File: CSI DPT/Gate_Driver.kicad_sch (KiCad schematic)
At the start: 21 parts, among them J1 CT3151SP-0, J2 CT3151SP-0, U1 UCC23513QDWYRQ1, U2 MGJ2D051802SC, U3 MGJ2D051802SC, U4 LDK130-12_SOT23_SOT353, U5 NC7SZ125M5X

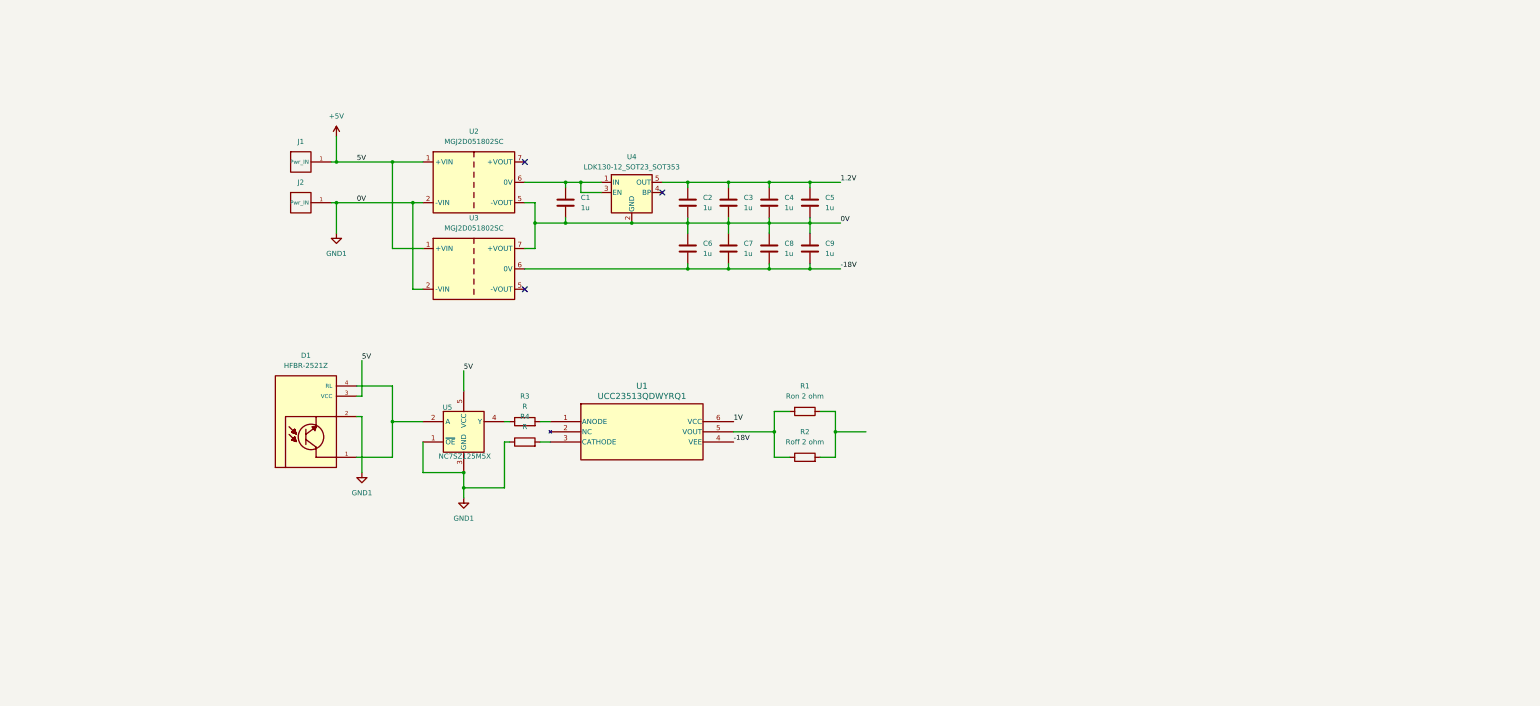
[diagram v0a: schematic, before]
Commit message: Nov.17 Update
Changed from opto PWM transmission to differential transmission. With added test point.
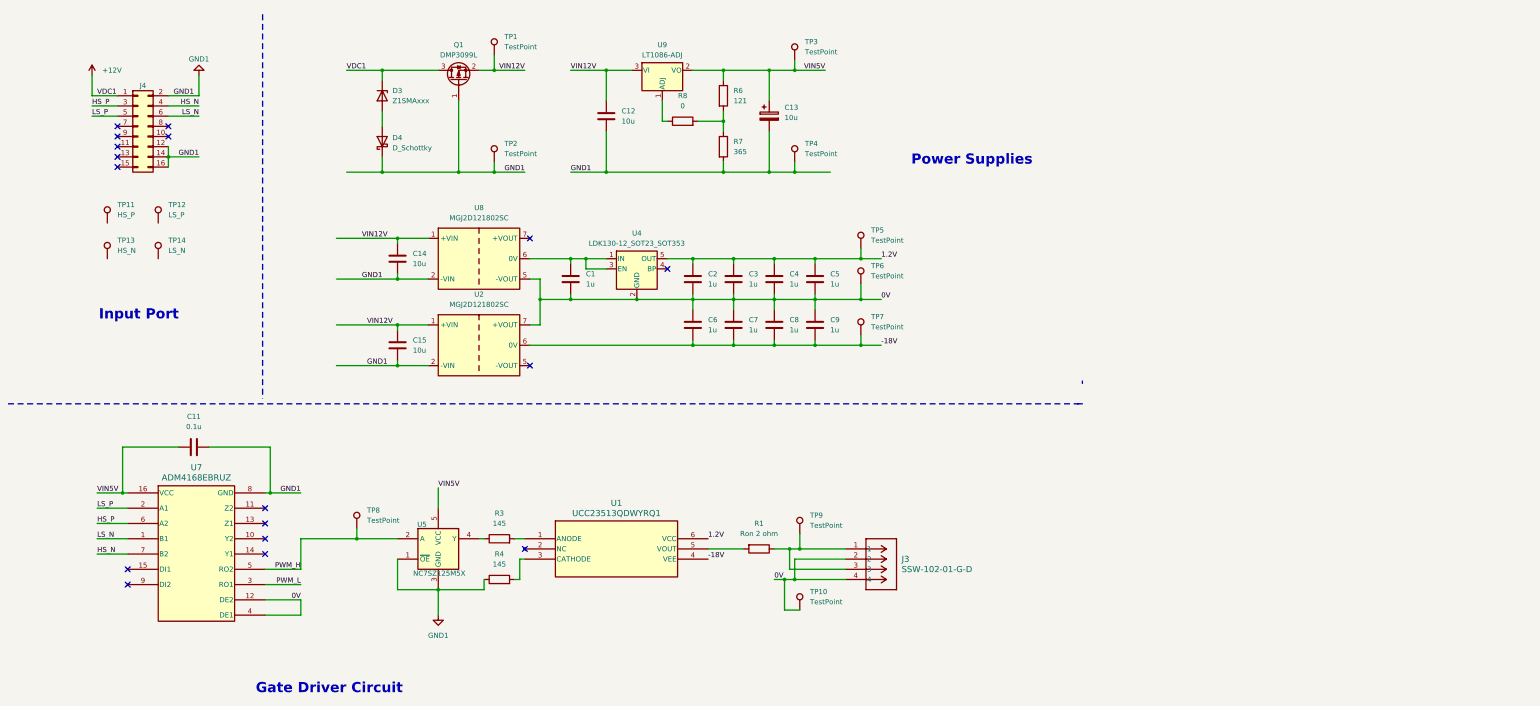
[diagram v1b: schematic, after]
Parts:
- removed D1: HFBR-2521Z, HFBR-2521Z:OPTO_HFBR-2521Z, symbol Opto_reciever:HFBR-2521Z
- removed J1, J2: CT3151SP-0, Connector:Banana_Jack_CT3151SP-0, symbol Connector:Banana_Jack_CT3151SP-0
- removed R2: Roff 2 ohm, symbol Device:R
- removed U2, U3: MGJ2D051802SC, Converter_DCDC:Converter_DCDC_Murata_MGJ2DxxxxxxSC_THT, symbol Converter_DCDC:MGJ2D051802SC
- added C11: 0.1u, symbol Device:C
- added C12: 10u, Capacitor_SMD:C_1206_3216Metric_Pad1.33x1.80mm_HandSolder, symbol Device:C
- added C13: 10u, symbol Device:C_Polarized
- added C14, C15: 10u, Capacitor_SMD:C_1206_3216Metric, symbol Device:C
- added D3: Z1SMAxxx, Diode_SMD:D_SMA_Handsoldering, symbol Diode:Z1SMAxxx
- added D4: D_Schottky, Diode_SMD:D_PowerDI-123, symbol Device:D_Schottky
- added J3: SSW-102-01-G-D, Gate_Driver:CON4_2X2_TU_SSQ, symbol 2*2_Gate_Driver_Output_Connector:SSW-102-01-G-D
- added J4: Conn_02x08_Odd_Even, Connector_IDC:IDC-Header_2x08_P2.54mm_Vertical, symbol Connector_Generic:Conn_02x08_Odd_Even
- added Q1: DMP3099L, Package_TO_SOT_SMD:SOT-23, symbol Transistor_FET:DMP3099L
- added R6: 121, Resistor_SMD:R_1206_3216Metric_Pad1.30x1.75mm_HandSolder, symbol Device:R
- added R7: 365, Resistor_SMD:R_1206_3216Metric_Pad1.30x1.75mm_HandSolder, symbol Device:R
- added R8: 0, Resistor_SMD:R_1206_3216Metric_Pad1.30x1.75mm_HandSolder, symbol Device:R
- added TP1: TestPoint, TestPoint:TestPoint_Pad_D2.0mm, symbol Connector:TestPoint
- added TP10, TP2, TP3, TP4, TP5, TP6, TP7, TP8, TP9: TestPoint, symbol Connector:TestPoint
- added TP11: HS_P, TestPoint:TestPoint_Pad_D2.0mm, symbol Connector:TestPoint
- added TP12: LS_P, TestPoint:TestPoint_Pad_D2.0mm, symbol Connector:TestPoint
- added TP13: HS_N, symbol Connector:TestPoint
- added TP14: LS_N, symbol Connector:TestPoint
- added U2, U8: MGJ2D121802SC, Converter_DCDC:Converter_DCDC_Murata_MGJ2DxxxxxxSC_THT, symbol Converter_DCDC:MGJ2D121802SC
- added U7: ADM4168EBRUZ, Gate_Driver:RU_16_ADI-M, symbol RS422_Transreciver:ADM4168EBRUZ
- added U9: LT1086-ADJ, symbol Regulator_Linear:LT1086-ADJ
- R1: footprint (none) -> Resistor_SMD:R_1206_3216Metric_Pad1.30x1.75mm_HandSolder
- R3, R4: value R -> 145; footprint Resistor_SMD:R_1206_3216Metric -> Resistor_SMD:R_1206_3216Metric_Pad1.30x1.75mm_HandSolder
- U1: footprint SOIC06_SO-6_7P5X4P68_TEX -> Gate_Driver:SOIC06_SO-6_7P5X4P68_TEX-M
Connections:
- net 1V is gone; now on net 1.2V: U1.6 (VCC)
- net -18V: now also TP7.1, U2.6 (0V)
- net 1.2V: now also TP5.1
- net GND1: now also C11.2, C12.2, C13.2, C14.2, C15.2, D4.1 (K), J4.12 (Pin_12), J4.14 (Pin_14), J4.16 (Pin_16), J4.2 (Pin_2), Q1.1 (G), R7.2, TP2.1, TP4.1, U2.2 (-VIN), U7.8 (GND), U8.2 (-VIN); no longer C1.2, C2.2, C3.2, C4.2, C5.2, C6.1, C7.1, C8.1, C9.1, U4.2 (GND)
- net at C1.1, U4.1 (IN), U4.3 (EN): now also U8.6 (0V)
- net at R1.1: now also J3.1, J3.3, TP9.1
- net PWM_H: now reaches U5.2 (A)
- net PWM_H: now also TP8.1, U7.5 (RO2)
- net +5V renamed VIN5V
- net VIN5V: now also C11.1, C13.1, R6.1, TP3.1, U7.16 (VCC), U9.2 (VO)
- new net: D3.2 (A), D4.2 (A)
- new net: R8.1, U9.1 (ADJ)
- new net: R6.2, R7.1, R8.2
- new net +12V: D3.1 (K), J4.1 (Pin_1), Q1.3 (D)
- new net 0V: C1.2, C2.2, C3.2, C4.2, C5.2, C6.1, C7.1, C8.1, C9.1, J3.2, J3.4, TP10.1, TP6.1, U2.7 (+VOUT), U4.2 (GND), U7.12 (DE2), U7.4 (DE1), U8.5 (-VOUT)
- new net HS_N: J4.4 (Pin_4), U7.7 (B2)
- new net HS_P: J4.3 (Pin_3), U7.6 (A2)
- new net LS_N: J4.6 (Pin_6), U7.1 (B1)
- new net LS_P: J4.5 (Pin_5), U7.2 (A1)
- new net PWM_L: U7.3 (RO1)
- new net VIN12V: C12.1, C14.1, C15.1, Q1.2 (S), TP1.1, U2.1 (+VIN), U8.1 (+VIN), U9.3 (VI)
- no-connect marks 3 -> 17
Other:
- note added: "Gate Driver Circuit"
- note added: "Input Port"
- note added: "Power Supplies"
- moved on the sheet: C1, C2, C3, C4, C5, C6, C7, C8, C9, R1, R3, R4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

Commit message: Nov.18 Update 1
temporary save
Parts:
- C11: footprint (none) -> Capacitor_SMD:C_1206_3216Metric_Pad1.33x1.80mm_HandSolder
- C13: footprint (none) -> Gate_Driver:TAJB_AVX-M
- TP10, TP13, TP14, TP2, TP3, TP4, TP5, TP6, TP7, TP8, TP9: footprint (none) -> TestPoint:TestPoint_Pad_D2.0mm
- U4: footprint (none) -> Package_TO_SOT_SMD:SOT-23-5_HandSoldering
- U5: footprint Package_TO_SOT_SMD:SOT-23-5 -> Package_TO_SOT_SMD:SOT-23-5_HandSoldering
- U9: footprint (none) -> Package_TO_SOT_SMD:TO-263-3_TabPin2
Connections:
- net 0V: no longer U7.12 (DE2), U7.4 (DE1)
- net GND1: now also U7.12 (DE2), U7.4 (DE1)

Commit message: Nov.18 Update 2
1. Finish PCB layout
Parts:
- added H1, H2, H3: MountingHole, MountingHole:MountingHole_4.3mm_M4_DIN965, symbol Mechanical:MountingHole
- renumbered TP7 to -18V1, TP10 to 0V1, TP6 to 0V2, TP5 to 1.2V1, TP2 to GND1A1, TP4 to GND1B1, TP13 to HS_N1, TP11 to HS_P1, TP14 to LS_N1, TP12 to LS_P1, TP8 to PWM_H1, TP9 to VGATE_H1, TP1 to VIN12V1, TP3 to VIN5V1
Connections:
- net HS_N: now also HS_N1.1
- net HS_P: now also HS_P1.1
- net LS_N: now also LS_N1.1
- net LS_P: now also LS_P1.1
- net VGATE_H: now reaches J3.1, J3.3, R1.1, VGATE_H1.1

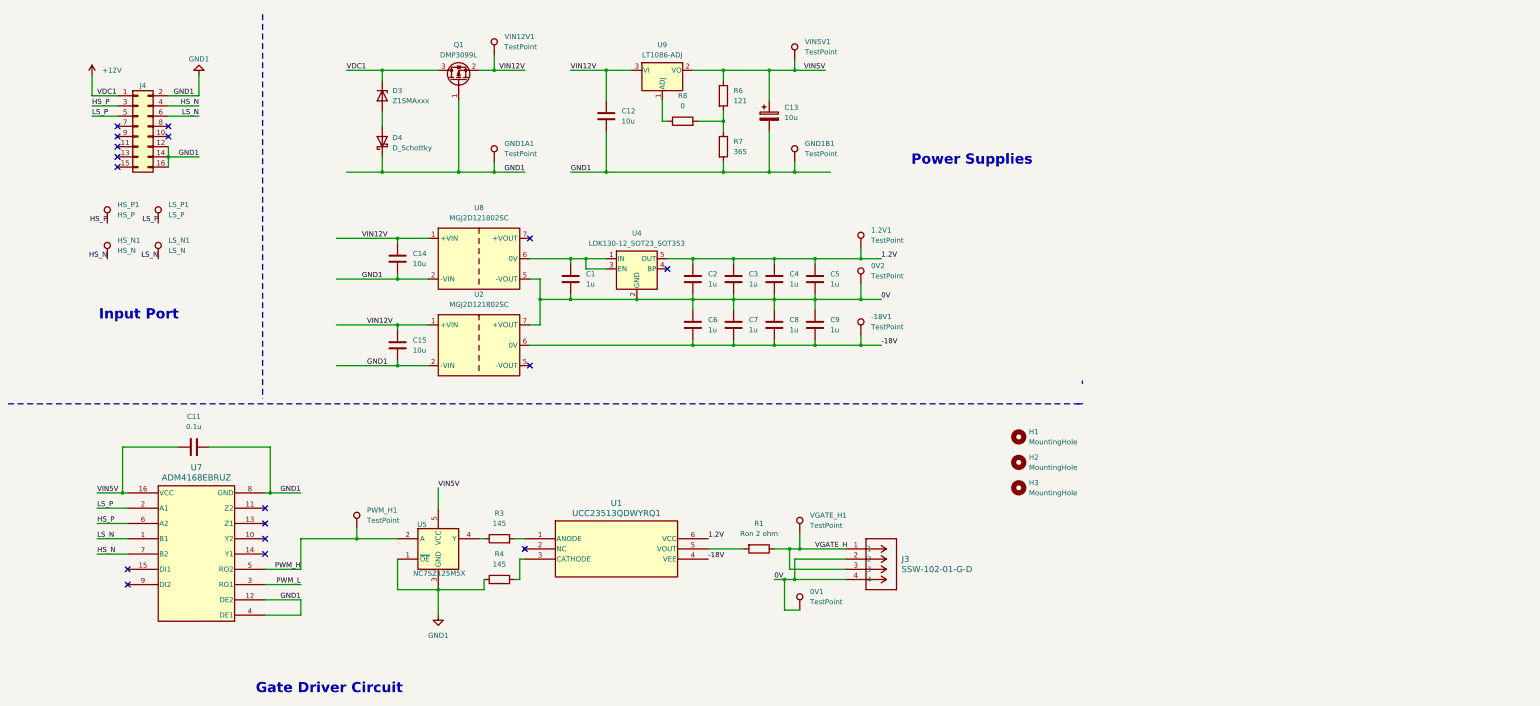
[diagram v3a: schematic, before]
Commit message: Gate Driver Complete
1. Competed half bridge gate driver
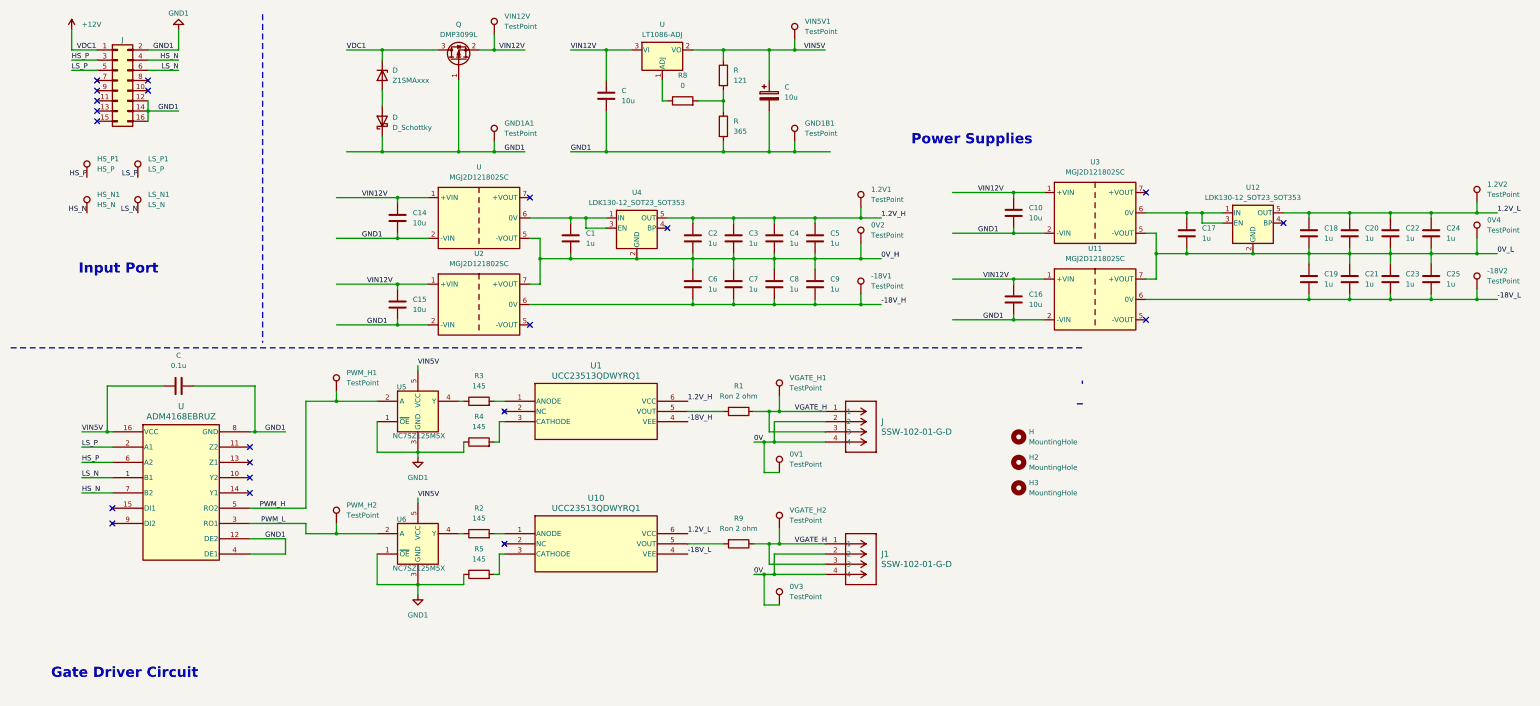
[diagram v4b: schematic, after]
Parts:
- added -18V2, 0V3, 0V4, 1.2V2, PWM_H2, VGATE_H2: TestPoint, TestPoint:TestPoint_Pad_D2.0mm, symbol Connector:TestPoint
- added C10, C16: 10u, Capacitor_SMD:C_1206_3216Metric, symbol Device:C
- added C17, C18, C19, C20, C21, C22, C23, C24, C25: 1u, Capacitor_SMD:C_1206_3216Metric, symbol Device:C
- added J1: SSW-102-01-G-D, Gate_Driver:CON4_2X2_TU_SSQ, symbol 2*2_Gate_Driver_Output_Connector:SSW-102-01-G-D
- added R2, R5: 145, Resistor_SMD:R_1206_3216Metric_Pad1.30x1.75mm_HandSolder, symbol Device:R_1206
- added R9: Ron 2 ohm, Resistor_SMD:R_1206_3216Metric_Pad1.30x1.75mm_HandSolder, symbol Device:R
- added U10: UCC23513QDWYRQ1, Gate_Driver:SOIC06_SO-6_7P5X4P68_TEX-M, symbol Gate_Driver:UCC23513QDWYRQ1
- added U11, U3: MGJ2D121802SC, Converter_DCDC:Converter_DCDC_Murata_MGJ2DxxxxxxSC_THT, symbol Converter_DCDC:MGJ2D121802SC
- added U12: LDK130-12_SOT23_SOT353, Package_TO_SOT_SMD:SOT-23-5_HandSoldering, symbol Regulator_Linear:LDK130-12_SOT23_SOT353
- added U6: NC7SZ125M5X, Package_TO_SOT_SMD:SOT-23-5_HandSoldering, symbol 74xGxx:NC7SZ125M5X
- renumbered C13 to C, C11 to C, C12 to C, D4 to D, D3 to D, H1 to H, J4 to J, J3 to J, Q1 to Q, R6 to R, R7 to R, U8 to U, U7 to U, U9 to U, VIN12V1 to VIN12V
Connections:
- net 0V: now also 0V3.1, J1.2, J1.4; no longer 0V2.1, C1.2, C2.2, C3.2, C4.2, C5.2, C6.1, C7.1, C8.1, C9.1, U.5 (-VOUT), U2.7 (+VOUT), U4.2 (GND)
- net GND1: now also C10.2, C16.2, R5.1, U11.2 (-VIN), U3.2 (-VIN), U6.1 (~{OE}), U6.3 (GND)
- net PWM_L: now also PWM_H2.1, U6.2 (A)
- net VGATE_H: now also J1.1, J1.3, R9.1, VGATE_H2.1
- net VIN12V: now also C10.1, C16.1, U11.1 (+VIN), U3.1 (+VIN)
- net VIN5V: now also U6.5 (VCC)
- net -18V renamed -18V_H
- net 1.2V renamed 1.2V_H
- new net: R5.2, U10.3 (CATHODE)
- new net: C17.1, U12.1 (IN), U12.3 (EN), U3.6 (0V)
- new net: R2.1, U6.4 (Y)
- new net: R2.2, U10.1 (ANODE)
- new net: R9.2, U10.5 (VOUT)
- new net -18V_L: -18V2.1, C19.2, C21.2, C23.2, C25.2, U10.4 (VEE), U11.6 (0V)
- new net 0V_H: 0V2.1, C1.2, C2.2, C3.2, C4.2, C5.2, C6.1, C7.1, C8.1, C9.1, U.5 (-VOUT), U2.7 (+VOUT), U4.2 (GND)
- new net 0V_L: 0V4.1, C17.2, C18.2, C19.1, C20.2, C21.1, C22.2, C23.1, C24.2, C25.1, U11.7 (+VOUT), U12.2 (GND), U3.5 (-VOUT)
- new net 1.2V_L: 1.2V2.1, C18.1, C20.1, C22.1, C24.1, U10.6 (VCC), U12.5 (OUT)
- no-connect marks 17 -> 21
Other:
- moved on the sheet: -18V1, 0V1, 0V2, 1.2V1, C, C1, C14, C15, C2, C3, C4, C5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

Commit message: test commit
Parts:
- renumbered C to C11, C to C12, C to C13, D to D3, D to D4, H to H1, J to J2, J to J3, PWM_H2 to PWM_L1, Q to Q3, R to R6, R to R7, U to U7, U to U8, U to U9, VIN12V to VIN12V1
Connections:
- net 0V_H is gone; now on net VSOURCE_H: 0V2.1, C1.2, C2.2, C3.2, C4.2, C5.2, C6.1, C7.1, C8.1, C9.1, U2.7 (+VOUT), U4.2 (GND), U8.5 (-VOUT)
- net VGATE_H: no longer J1.1, J1.3, R9.1, VGATE_H2.1
- net 0V renamed VSOURCE_H
- net VSOURCE_H: no longer 0V3.1, J1.2, J1.4
- net 0V_L renamed VSOURCE_L
- net VSOURCE_L: now also 0V3.1, J1.2, J1.4
- new net VGATE_L: J1.1, J1.3, R9.1, VGATE_H2.1
